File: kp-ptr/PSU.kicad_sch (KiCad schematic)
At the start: 22 parts, among them J2 Conn_01x02, J3 Conn_01x02, U8 LM1117-5.0

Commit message: 1 próba pomieszczenia wszystkiego
Signed-off-by: kretu <krecik@gmail.com>
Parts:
- J2: footprint TerminalBlock_Phoenix:TerminalBlock_Phoenix_MPT-0,5-2-2.54_1x02_P2.54mm_Horizontal -> Connector_JST:JST_GH_SM02B-GHS-TB_1x02-1MP_P1.25mm_Horizontal
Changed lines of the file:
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@@
     (property "Reference" "J2" (id 0) (at 21.59 38.1 0))
     (property "Value" "Conn_01x02" (id 1) (at 21.59 40.64 0))
-    (property "Footprint" "TerminalBlock_Phoenix:TerminalBlock_Phoenix_MPT-0,5-2-2.54_1x02_P2.54mm_Horizontal" (id 2) (at 21.59 46.99 0)
+    (property "Footprint" "Connector_JST:JST_GH_SM02B-GHS-TB_1x02-1MP_P1.25mm_Horizontal" (id 2) (at 21.59 46.99 0)
       (effects (font (size 1.27 1.27)) hide)
     )

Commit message: swiatelko w tunelu aby zmiescic wszystko
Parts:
- J2: footprint Connector_JST:JST_GH_SM02B-GHS-TB_1x02-1MP_P1.25mm_Horizontal -> TerminalBlock_TE-Connectivity:TerminalBlock_TE_282834-2_1x02_P2.54mm_Horizontal
- J3: footprint TerminalBlock_Phoenix:TerminalBlock_Phoenix_MPT-0,5-2-2.54_1x02_P2.54mm_Horizontal -> TerminalBlock_TE-Connectivity:TerminalBlock_TE_282834-2_1x02_P2.54mm_Horizontal
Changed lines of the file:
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@@
     (property "Reference" "J2" (id 0) (at 21.59 38.1 0))
     (property "Value" "Conn_01x02" (id 1) (at 21.59 40.64 0))
-    (property "Footprint" "Connector_JST:JST_GH_SM02B-GHS-TB_1x02-1MP_P1.25mm_Horizontal" (id 2) (at 21.59 46.99 0)
+    (property "Footprint" "TerminalBlock_TE-Connectivity:TerminalBlock_TE_282834-2_1x02_P2.54mm_Horizontal" (id 2) (at 21.59 46.99 0)
       (effects (font (size 1.27 1.27)) hide)
     )
@@
       (effects (font (size 1.27 1.27)) (justify right))
     )
-    (property "Footprint" "TerminalBlock_Phoenix:TerminalBlock_Phoenix_MPT-0,5-2-2.54_1x02_P2.54mm_Horizontal" (id 2) (at 42.545 49.53 0)
+    (property "Footprint" "TerminalBlock_TE-Connectivity:TerminalBlock_TE_282834-2_1x02_P2.54mm_Horizontal" (id 2) (at 42.545 49.53 0)
       (effects (font (size 1.27 1.27)) hide)
     )

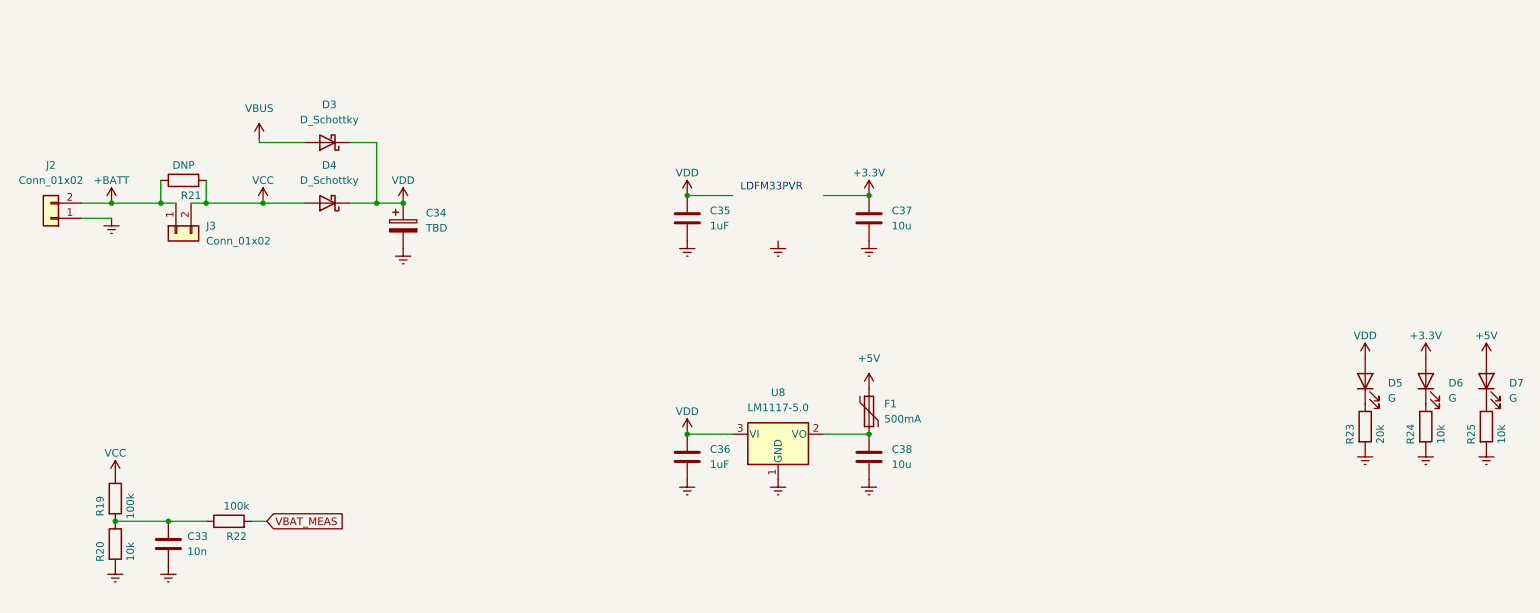
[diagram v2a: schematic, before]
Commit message: chyba wszystkie footprinty
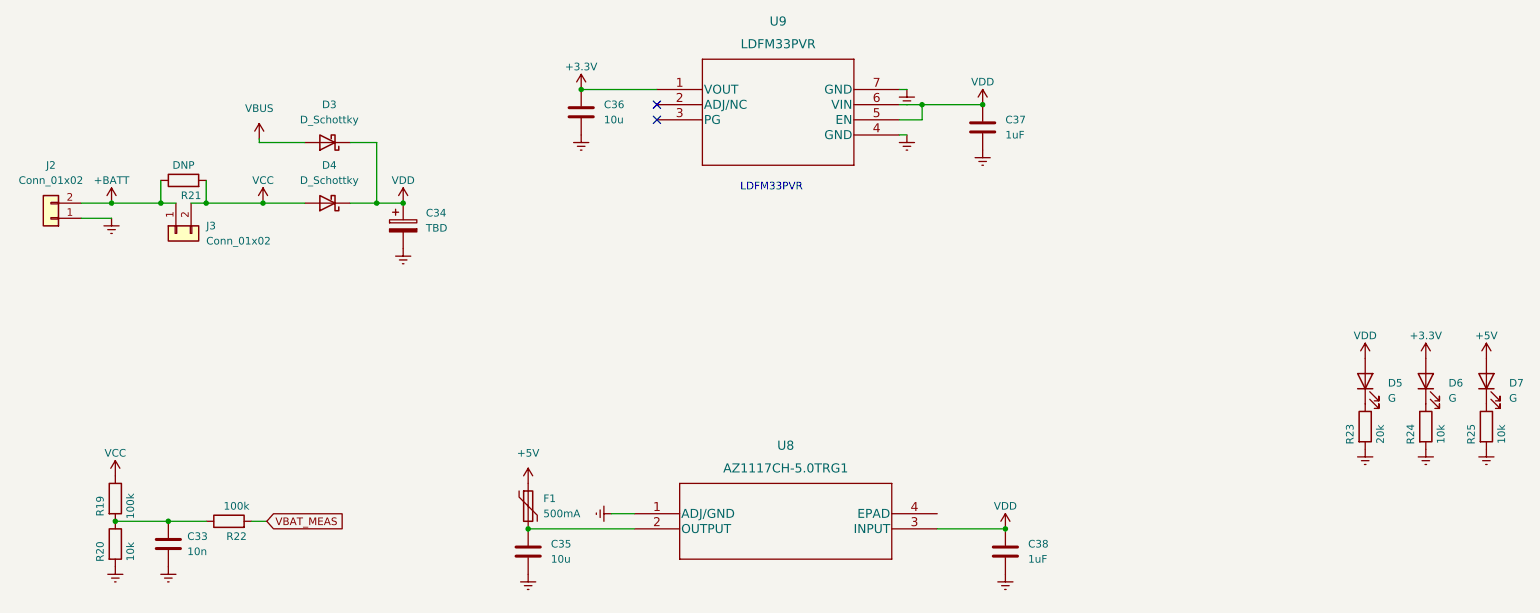
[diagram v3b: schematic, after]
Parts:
- removed U8: LM1117-5.0, symbol Regulator_Linear:LM1117-5.0
- added U8: AZ1117CH-5.0TRG1, KP-PTR_lib:AZ1117CH-5.0TRG1, symbol KP-PTR_lib:AZ1117CH-5.0TRG1
- added U9: LDFM33PVR, KP-PTR_lib:LDFM33PVR, symbol KP-PTR_lib:LDFM33PVR
- renumbered C38 to C35, C37 to C36, C35 to C37, C36 to C38
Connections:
- net +3V3: now also U9.1 (VOUT)
- net Earth: now also U8.1 (ADJ/GND), U9.4 (GND), U9.7 (GND)
- net VDD: now also U8.3 (INPUT), U9.5 (EN), U9.6 (VIN)
- net at C35.1, F1.2: now also U8.2 (OUTPUT)
- no-connect marks 0 -> 2
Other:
- moved on the sheet: C35, C36, C37, C38, F1

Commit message: PCB update
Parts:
- C34: footprint Capacitor_SMD:C_0402_1005Metric -> Capacitor_SMD:CP_Elec_10x10
- R21: footprint Resistor_SMD:R_0402_1005Metric -> Resistor_SMD:R_1206_3216Metric
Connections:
- net +BATT: now also J3.2 (Pin_2); no longer J3.1 (Pin_1)
- net VCC: now also C38.1, J3.1 (Pin_1), U8.3 (INPUT); no longer J3.2 (Pin_2)
- net VDD: no longer C38.1, U8.3 (INPUT)
- net at C35.1, F1.2, U8.2 (OUTPUT): now also U8.4 (EPAD)
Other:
- moved on the sheet: C35, C38, F1, J3, U8

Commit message: SCH&PCB update
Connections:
- net +BATT: now also J2.1 (Pin_1); no longer J2.2 (Pin_2)
- net Earth: now also J2.2 (Pin_2); no longer J2.1 (Pin_1)
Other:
- moved on the sheet: C36, C37, J2, U9

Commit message: Release v0.1
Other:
- company: (none) -> Polskie Towarzystwo Rakietowe
- title: (none) -> KP-PTR
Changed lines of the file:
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@@
 (kicad_sch (version 20211123) (generator eeschema)
   (paper "A4")
+  (title_block
+    (title "KP-PTR")
+    (date "2022-06-29")
+    (rev "0.1")
+    (company "Polskie Towarzystwo Rakietowe")
+    (comment 1 "bartekM, FlyingBanana, Kretu, Red Labs, Stachu M, U.S. air force i inni")
+  )
   (junction (at 41.275 97.79) (diameter 0) (color 0 0 0 0)
   )
